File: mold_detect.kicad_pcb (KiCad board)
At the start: 2 copper layers, 37 x 70 mm, 26 parts, among them J1 USB_C_Receptacle_USB2.0_14P, U1 SHT30-DIS, U2 TPL5010, U3 ATmega328P-P, U4 W25Q128JVS, U5 FT230XS

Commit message: the spi flash chip works
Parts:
- added C10: 22pF, Capacitor_SMD:C_0603_1608Metric_Pad1.08x0.95mm_HandSolder, F.Cu at (123.5, 72.5)
- added C2: 47pF, Capacitor_SMD:C_0603_1608Metric_Pad1.08x0.95mm_HandSolder, F.Cu at (123.5, 57.4)
- added C3: 10nF, Capacitor_SMD:C_0603_1608Metric_Pad1.08x0.95mm_HandSolder, F.Cu at (123.5, 59.9)
- added C4: 47pF, Capacitor_SMD:C_0603_1608Metric_Pad1.08x0.95mm_HandSolder, F.Cu at (123.5, 62.4)
- added C5: 100n, Capacitor_SMD:C_0603_1608Metric_Pad1.08x0.95mm_HandSolder, F.Cu at (123.5, 64.9)
- added C6: 100n, Capacitor_SMD:C_0603_1608Metric_Pad1.08x0.95mm_HandSolder, F.Cu at (123.5, 67.4)
- added C9: 22pF, Capacitor_SMD:C_0603_1608Metric_Pad1.08x0.95mm_HandSolder, F.Cu at (123.5, 69.9)
- added R6: 27R, Resistor_SMD:R_0603_1608Metric_Pad0.98x0.95mm_HandSolder, F.Cu at (123.5, 75.0)
- added R7: 27R, Resistor_SMD:R_0603_1608Metric_Pad0.98x0.95mm_HandSolder, F.Cu at (123.5, 77.5)
- C3: value 100n -> 10nF
- renumbered C2 to C8, R6 to R10, R7 to R4, R8 to R5, R4 to R8, R5 to R9, U5 to U3, U3 to U5
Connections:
- C3 pad 2: +3V0 -> Net-(C3-Pad2)
- J1 pad A4: Net-(U5-VCC) -> Net-(C3-Pad2)
- J1 pad A6: Net-(U5-USBDM) -> Net-(C4-Pad2)
- J1 pad A7: Net-(U5-USBDP) -> Net-(C2-Pad2)
- J1 pad A9: Net-(U5-VCC) -> Net-(C3-Pad2)
- J1 pad B4: Net-(U5-VCC) -> Net-(C3-Pad2)
- J1 pad B6: Net-(U5-USBDM) -> Net-(C4-Pad2)
- J1 pad B7: Net-(U5-USBDP) -> Net-(C2-Pad2)
- J1 pad B9: Net-(U5-VCC) -> Net-(C3-Pad2)
- U3 pad 1: TXD -> RXD
- U3 pad 11: unconnected-(U5-~{RESET}-Pad11) -> +3V0
- U3 pad 12: Net-(U5-VCC) -> Net-(U3-VCC)
- U3 pad 4: RXD -> TXD
- U3 pad 8: Net-(U5-USBDP) -> Net-(U3-USBDP)
- U3 pad 9: Net-(U5-USBDM) -> Net-(U3-USBDM)
- U5 pad 10: unconnected-(U3-XTAL2/PB7-Pad10) -> Net-(U5-XTAL2/PB7)
- U5 pad 9: unconnected-(U3-XTAL1/PB6-Pad9) -> Net-(U5-XTAL1/PB6)
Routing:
- net (no net): track 0.00 -> 40.2 mm, vias 0 -> 2
- net Net-(U5-VCC): track 16.3 -> 0.00 mm, vias 2 -> 0
- net Net-(U5-USBDP): track 13.2 -> 0.00 mm
- net Net-(U5-USBDM): track 10.7 -> 0.00 mm

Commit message: tpl5010 works!
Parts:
- added C11: 100n, Capacitor_SMD:C_0603_1608Metric_Pad1.08x0.95mm_HandSolder, F.Cu at (141.6, 116.5)
- added D2: D_Schottky, Diode_SMD:D_SOD-323_HandSoldering, F.Cu at (142.0, 113.8)
- added J2: ISP, Connector_IDC:IDC-Header_2x03_P2.54mm_Vertical, F.Cu at (128.0, 112.0)
- added R11: 100R, Resistor_SMD:R_0603_1608Metric_Pad0.98x0.95mm_HandSolder, F.Cu at (141.6, 119.0)
- added Red2: LED, LED_THT:LED_D3.0mm, F.Cu at (141.1, 109.5)
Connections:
- net MISO renamed CIPO
- net MOSI renamed COPI
- Blue1 pad 2: TEMP_LED -> HUM_LED
- C3 pad 2: Net-(C3-Pad2) -> Net-(D2-K) (x2)
- J1 pad A4: Net-(C3-Pad2) -> Net-(D2-A)
- J1 pad A9: Net-(C3-Pad2) -> Net-(D2-A)
- J1 pad B4: Net-(C3-Pad2) -> Net-(D2-A)
- J1 pad B9: Net-(C3-Pad2) -> Net-(D2-A)
- R1 pad 1: Net-(Red1-K) -> GND
- R1 pad 2: GND -> Net-(Red2-K)
- R2 pad 1: Net-(Blue1-K) -> GND
- R2 pad 2: GND -> Net-(Blue1-K)
- Red1 pad 2: HUM_LED -> ERROR_LED
- U5 pad 13: unconnected-(U5-PD7-Pad13) -> ERROR_LED
- U5 pad 15: FLASH_CS -> unconnected-(U5-PB1-Pad15)
- U5 pad 16: unconnected-(U5-PB2-Pad16) -> FLASH_CS
- U5 pad 4: WAKE_INTR -> unconnected-(U5-PD2-Pad4)
- U5 pad 5: DONE -> WAKE_INTR
- U5 pad 6: unconnected-(U5-PD4-Pad6) -> DONE
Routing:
- net Net-(U3-VCC): track 0.00 -> 16.3 mm, vias 0 -> 2
- net (no net): track 40.2 -> 23.9 mm, vias 2 -> 0

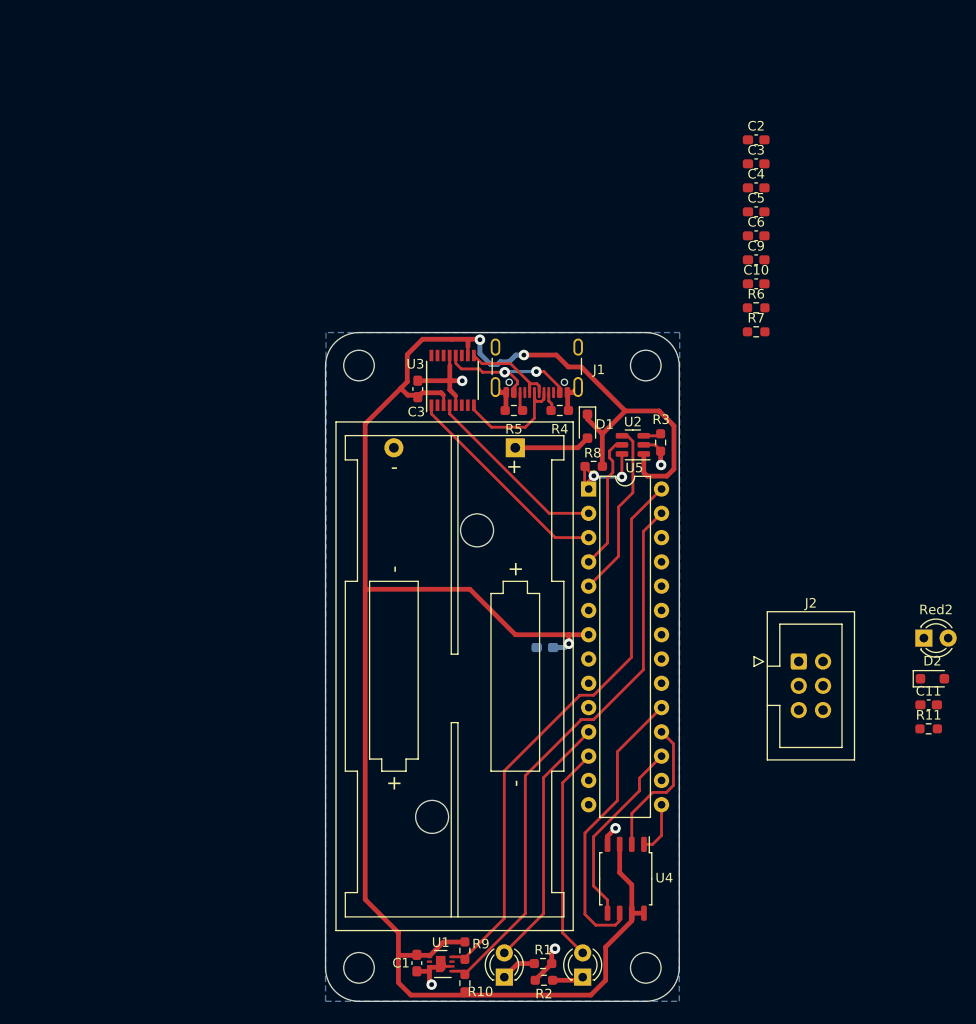
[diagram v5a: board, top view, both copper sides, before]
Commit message: updated footprints; started layout
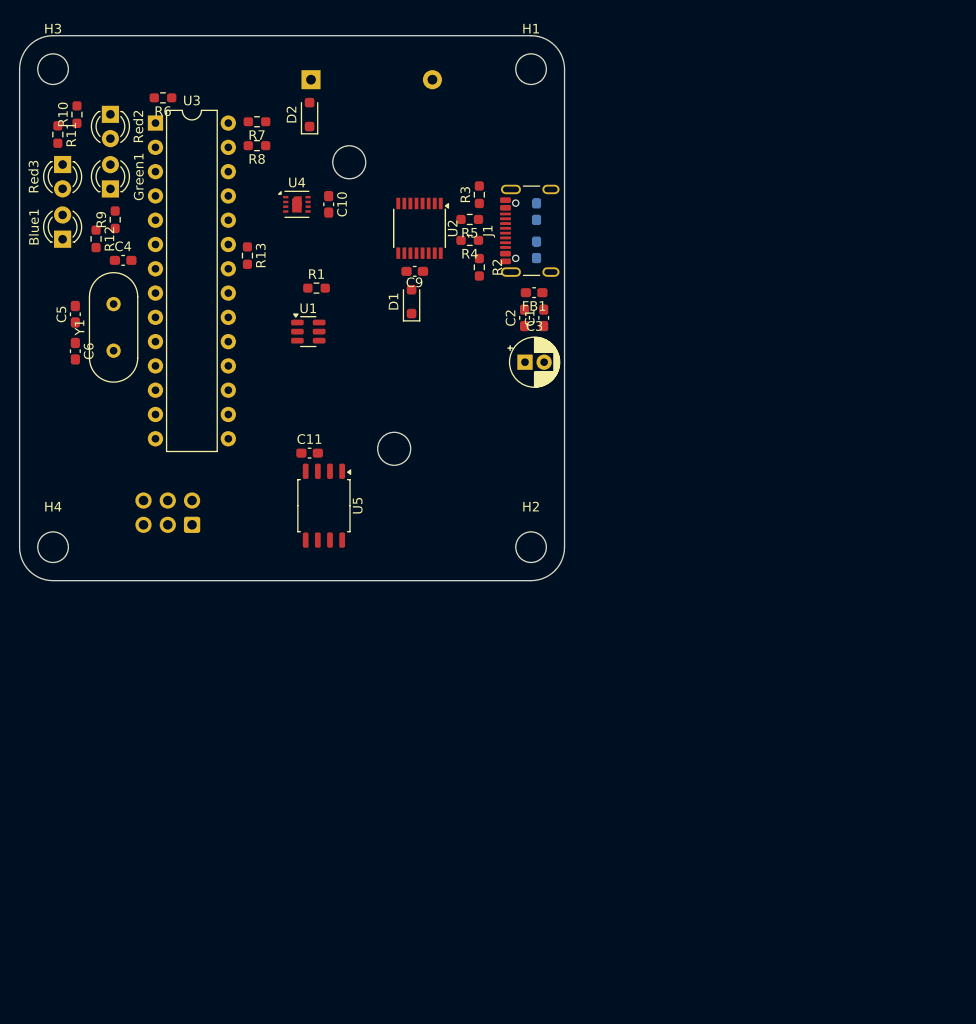
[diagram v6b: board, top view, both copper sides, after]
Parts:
- removed the C3 at (88.2, 83.5)
- removed the C3 at (123.5, 59.9)
- removed G***: LOGO, Library:kit_logo
- removed Red1: LED, LED_THT:LED_D3.0mm
- added C3: 4u7, Capacitor_THT:CP_Radial_D5.0mm_P2.00mm, F.Cu at (99.4, 80.7)
- added C7: 47pF, Capacitor_SMD:C_0603_1608Metric_Pad1.08x0.95mm_HandSolder, B.Cu at (100.6, 64.9)
- added FB1: ~, Capacitor_SMD:C_0603_1608Metric_Pad1.08x0.95mm_HandSolder, F.Cu at (100.3, 73.4)
- added Green1: LED, LED_THT:LED_D3.0mm, F.Cu at (56.0, 62.5)
- added R12: 100R, Resistor_SMD:R_0603_1608Metric_Pad0.98x0.95mm_HandSolder, F.Cu at (54.5, 67.8)
- added R13: 10k, Resistor_SMD:R_0603_1608Metric_Pad0.98x0.95mm_HandSolder, F.Cu at (70.3, 69.5)
- added Red3: LED, LED_THT:LED_D3.0mm, F.Cu at (51.0, 60.0)
- added Y1: 16MHz, Crystal:Crystal_HC49-4H_Vertical, F.Cu at (56.3, 79.5)
- BT1, J2: moved to B.Cu
- C1: value 100n -> 10nF
- C10, C9: value 22pF -> 100n
- C2, C4: value 47pF -> 100n
- C5, C6: value 100n -> 22pF
- C8: value 100n -> 47pF
- R1: value 100R -> 22k021
- R10, R9: value 10k -> 100R
- R2: value 100R -> 5k1
- R3: value 22k021 -> 5k1
- R4, R5: value 5k1 -> 27R
- R6, R7: value 27R -> 10k
- U1: value SHT30-DIS -> TPL5010; footprint Sensor_Humidity:Sensirion_DFN-8-1EP_2.5x2.5mm_P0.5mm_EP1.1x1.7mm -> Package_TO_SOT_SMD:SOT-23-6
- U2: value TPL5010 -> FT230XS; footprint Package_TO_SOT_SMD:SOT-23-6 -> Package_SO:SSOP-16_3.9x4.9mm_P0.635mm
- U3: value FT230XS -> ATmega328P-P; footprint Package_SO:SSOP-16_3.9x4.9mm_P0.635mm -> Package_DIP:DIP-28_W7.62mm
- U4: value W25Q128JVS -> SHT30-DIS; footprint Package_SO:SOIC-8_5.23x5.23mm_P1.27mm -> Sensor_Humidity:Sensirion_DFN-8-1EP_2.5x2.5mm_P0.5mm_EP1.1x1.7mm
- U5: value ATmega328P-P -> W25Q128JVS; footprint Package_DIP:DIP-28_W7.62mm -> Package_SO:SOIC-8_5.23x5.23mm_P1.27mm
- moved H3 112.6 mm to (50.0, 50.0)
- moved R11 110.3 mm to (50.5, 56.8), turned to -90 degrees
- moved Red2 101.2 mm to (56.0, 54.7), turned to -90 degrees
- moved R10 99.5 mm to (52.5, 54.8)
- moved H1 95.7 mm to (100.0, 50.0)
- moved Blue1 94.4 mm to (51.0, 67.8)
- moved D2 87.9 mm to (76.8, 54.8), turned to 90 degrees
- moved R9 84.7 mm to (56.5, 65.8), turned to 90 degrees
- moved U4 78.5 mm to (75.5, 64.1), turned to 0 degrees
- moved R2 74.9 mm to (94.6, 70.7), turned to -90 degrees
- moved R1 74.5 mm to (77.6, 72.9)
- moved C6 72.2 mm to (52.3, 79.5), turned to -90 degrees
- moved C5 72.0 mm to (52.3, 75.6), turned to 90 degrees
- moved C11 69.9 mm to (76.8, 90.2)
- moved C1 68.8 mm to (101.3, 76.0)
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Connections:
- C1 pad 2: +3V0 -> Net-(C1-Pad2)
- C10 pad 2: Net-(U5-XTAL2/PB7) -> +3V0
- C2 pad 2: Net-(C2-Pad2) -> Net-(U2-VCC)
- C4 pad 2: Net-(C4-Pad2) -> +3V0
- C5 pad 2: +3V0 -> Net-(U3-XTAL1/PB6)
- C6 pad 2: Net-(U3-VCC) -> Net-(U3-XTAL2/PB7)
- C8 pad 2: +3V0 -> Net-(C8-Pad2)
- C9 pad 2: Net-(U5-XTAL1/PB6) -> USB_ENABLE_INTR
- D1 pad 2: Net-(BT1-+) -> USB_ENABLE_INTR
- D2 pad 1: Net-(D2-K) -> +3V0
- D2 pad 2: Net-(D2-A) -> Net-(BT1-+)
- J1 pad A4: Net-(D2-A) -> Net-(C1-Pad2)
- J1 pad A6: Net-(C4-Pad2) -> Net-(C8-Pad2)
- J1 pad A7: Net-(C2-Pad2) -> Net-(C7-Pad2)
- J1 pad A9: Net-(D2-A) -> Net-(C1-Pad2)
- J1 pad B4: Net-(D2-A) -> Net-(C1-Pad2)
- J1 pad B6: Net-(C4-Pad2) -> Net-(C8-Pad2)
- J1 pad B7: Net-(C2-Pad2) -> Net-(C7-Pad2)
- J1 pad B9: Net-(D2-A) -> Net-(C1-Pad2)
- R1 pad 1: GND -> Net-(U1-DELAY/M_RST)
- R1 pad 2: Net-(Red2-K) -> GND
- R10 pad 1: +3V0 -> GND
- R10 pad 2: SDA -> Net-(Red2-K)
- R2 pad 1: GND -> Net-(J1-CC1)
- R2 pad 2: Net-(Blue1-K) -> GND
- R3 pad 1: Net-(U2-DELAY/M_RST) -> Net-(J1-CC2)
- R4 pad 1: Net-(J1-CC1) -> Net-(C7-Pad2)
- R4 pad 2: GND -> Net-(U2-USBDM)
- R5 pad 1: Net-(J1-CC2) -> Net-(C8-Pad2)
- R5 pad 2: GND -> Net-(U2-USBDP)
- R6 pad 1: Net-(C2-Pad2) -> +3V0
- R6 pad 2: Net-(U3-USBDM) -> RST
- R7 pad 1: Net-(C4-Pad2) -> +3V0
- R7 pad 2: Net-(U3-USBDP) -> SCL
- R8 pad 2: RST -> SDA
- R9 pad 1: +3V0 -> GND
- R9 pad 2: SCL -> Net-(Green1-K)
- Red2 pad 2: TEMP_LED -> ERROR_LED
- U1 pad 1: SDA -> +3V0
- U1 pad 3: unconnected-(U1-ALERT-Pad3) -> Net-(U1-DELAY/M_RST)
- U1 pad 4: SCL -> DONE
- U1 pad 5: +3V0 -> WAKE_INTR
- U1 pad 6: unconnected-(U1-~{RESET}-Pad6) -> RST
- U2 pad 1: +3V0 -> RXD
- U2 pad 2: GND -> unconnected-(U2-~{RTS}-Pad2)
- U2 pad 3: Net-(U2-DELAY/M_RST) -> USB_ENABLE_INTR
- U2 pad 4: DONE -> TXD
- U2 pad 5: WAKE_INTR -> GND
- U2 pad 6: RST -> unconnected-(U2-~{CTS}-Pad6)
- U3 pad 1: RXD -> RST
- U3 pad 10: +3V0 -> Net-(U3-XTAL2/PB7)
- U3 pad 11: +3V0 -> HUM_LED
- U3 pad 12: Net-(U3-VCC) -> TEMP_LED
- U3 pad 13: GND -> ERROR_LED
- U3 pad 16: unconnected-(U3-CBUS3-Pad16) -> FLASH_CS
- U3 pad 2: unconnected-(U3-~{RTS}-Pad2) -> RXD
- U3 pad 3: +3V0 -> TXD
- U3 pad 4: TXD -> GENERAL_LED
- U3 pad 5: GND -> WAKE_INTR
- U3 pad 6: unconnected-(U3-~{CTS}-Pad6) -> DONE
- U3 pad 7: unconnected-(U3-CBUS2-Pad7) -> +3V0
- U3 pad 8: Net-(U3-USBDP) -> GND
- U3 pad 9: Net-(U3-USBDM) -> Net-(U3-XTAL1/PB6)
- U4 pad 1: FLASH_CS -> SDA
- U4 pad 2: CIPO -> GND
- U4 pad 3: +3V0 -> unconnected-(U4-ALERT-Pad3)
- U4 pad 4: GND -> SCL
- U4 pad 5: COPI -> +3V0
- U4 pad 6: SCK -> unconnected-(U4-~{RESET}-Pad6)
- U4 pad 7: +3V0 -> GND
- U4 pad 8: +3V0 -> GND
- U5 pad 1: RST -> FLASH_CS
- U5 pad 2: RXD -> CIPO
- U5 pad 3: TXD -> +3V0
- U5 pad 4: unconnected-(U5-PD2-Pad4) -> GND
- U5 pad 5: WAKE_INTR -> COPI
- U5 pad 6: DONE -> SCK
- U5 pad 8: GND -> +3V0
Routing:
- net +3V0: track 206.1 -> 0.00 mm, vias 3 -> 0
- net SCL: track 60.0 -> 0.00 mm
- net SDA: track 58.9 -> 0.00 mm
- net GND: track 32.7 -> 0.00 mm, vias 5 -> 0
- net SCK: track 30.0 -> 0.00 mm
- net HUM_LED: track 26.8 -> 0.00 mm
- net (no net): track 23.9 -> 0.00 mm
- net TXD: track 22.8 -> 0.00 mm
- net TEMP_LED: track 22.6 -> 0.00 mm
- net COPI: track 20.0 -> 0.00 mm
- net RXD: track 19.8 -> 0.00 mm
- net DONE: track 18.8 -> 0.00 mm
- net Net-(U3-VCC): track 16.3 -> 0.00 mm, vias 2 -> 0
- net CIPO: track 14.9 -> 0.00 mm
- net WAKE_INTR: track 14.4 -> 0.00 mm
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- removed copper zone on B.Cu, net GND
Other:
- board size 37 x 70 mm -> 57 x 57 mm
- board text removed: "github.com/christopher-besch/mold_detect Christopher Besch <mail@chris-besch.com> designed at the Chair for Embedded Systems Rev. 1.0.0 January 2024"

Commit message: updated PCB design
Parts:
- removed Red3: LED, LED_THT:LED_D3.0mm
- added C12: 100n, Capacitor_SMD:C_0603_1608Metric_Pad1.08x0.95mm_HandSolder, F.Cu at (82.5, 81.0)
- added G***: LOGO, Library:kit_logo, B.Cu at (95.0, 93.5)
- added Red1: LED, LED_THT:LED_D3.0mm, F.Cu at (51.0, 60.0)
- C5: value 22pF -> 100n; moved to B.Cu
- C7: value 47pF -> 22pF; moved to F.Cu
- C9: value 100n -> 47pF; moved to B.Cu
- J2: moved to F.Cu
- R13: value 10k -> 100R
- R9: value 100R -> 10k
- moved C7 50.1 mm to (52.7, 79.5)
- moved C11 33.7 mm to (74.5, 56.5), turned to 90 degrees
- moved C4 19.4 mm to (76.5, 73.0)
- moved R6 18.9 mm to (70.5, 69.6), turned to -90 degrees
- moved R9 16.9 mm to (71.5, 58.0), turned to 180 degrees
- moved R13 16.0 mm to (54.5, 67.5)
- moved C9 14.1 mm to (100.5, 65.0), turned to -90 degrees
- moved U5 13.1 mm to (76.9, 82.6), turned to 180 degrees
- moved R12 12.5 mm to (52.5, 55.4), turned to 90 degrees
- moved C5 11.8 mm to (63.5, 71.9)
- moved R10 11.5 mm to (56.5, 65.5)
- moved C10 11.5 mm to (88.0, 71.0), turned to 180 degrees
- moved R7 10.1 mm to (61.5, 53.0)
- moved U4 8.18 mm to (77.7, 56.2), turned to 180 degrees
- moved J2 5.05 mm to (59.5, 98.0)
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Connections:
- C10 pad 2: +3V0 -> USB_ENABLE_INTR
- C5 pad 2: Net-(U3-XTAL1/PB6) -> +3V0
- C6 pad 2: Net-(U3-XTAL2/PB7) -> Net-(U3-XTAL1/PB6)
- C7 pad 2: Net-(C7-Pad2) -> Net-(U3-XTAL2/PB7)
- C9 pad 2: USB_ENABLE_INTR -> Net-(C9-Pad2)
- J1 pad A6: Net-(C8-Pad2) -> Net-(C9-Pad2)
- J1 pad A7: Net-(C7-Pad2) -> Net-(C8-Pad2)
- J1 pad B6: Net-(C8-Pad2) -> Net-(C9-Pad2)
- J1 pad B7: Net-(C7-Pad2) -> Net-(C8-Pad2)
- R10 pad 2: Net-(Red2-K) -> Net-(Green1-K)
- R12 pad 2: Net-(Blue1-K) -> Net-(Red2-K)
- R13 pad 1: USB_ENABLE_INTR -> GND
- R13 pad 2: GND -> Net-(Blue1-K)
- R4 pad 1: Net-(C7-Pad2) -> Net-(C8-Pad2)
- R5 pad 1: Net-(C8-Pad2) -> Net-(C9-Pad2)
- R6 pad 1: +3V0 -> USB_ENABLE_INTR
- R6 pad 2: RST -> GND
- R7 pad 2: SCL -> RST
- R8 pad 2: SDA -> SCL
- R9 pad 1: GND -> +3V0
- R9 pad 2: Net-(Green1-K) -> SDA
- Red2 pad 2: ERROR_LED -> TEMP_LED
- U3 pad 11: HUM_LED -> GENERAL_LED
- U3 pad 12: TEMP_LED -> HUM_LED
- U3 pad 4: GENERAL_LED -> TEMP_LED
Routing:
- net +3V0: track 0.00 -> 135.4 mm, vias 0 -> 7
- net RST: track 0.00 -> 82.8 mm, vias 0 -> 4
- net GND: track 0.00 -> 55.3 mm, vias 0 -> 7
- net GENERAL_LED: track 0.00 -> 35.9 mm
- net SCK: track 0.00 -> 35.9 mm
- net CIPO: track 0.00 -> 35.7 mm
- net ERROR_LED: track 0.00 -> 34.3 mm
- net COPI: track 0.00 -> 33.1 mm, vias 0 -> 2
- net RXD: track 0.00 -> 32.8 mm
- net USB_ENABLE_INTR: track 0.00 -> 30.6 mm, vias 0 -> 2
- net TXD: track 0.00 -> 29.9 mm
- net HUM_LED: track 0.00 -> 29.0 mm
- net WAKE_INTR: track 0.00 -> 27.3 mm
- net DONE: track 0.00 -> 26.0 mm
- net Net-(U2-VCC): track 0.00 -> 21.8 mm
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- added copper zone on F.Cu, net (none)
- added copper zone on B.Cu, net GND
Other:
- board text added: "ISP"
- board text added: "Rev. 2.0.0 April 2024"
- board text added: "USB-C"
- board text added: "designed at the Chair for Embedded Systems"
- board text added: "github.com/christopher-besch/mold_detect"
- board text added: "made in Germany by Christopher Besch <mail@chris-besch.com>"

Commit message: added blender
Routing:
- added copper zone on F.Cu, net GND
- removed copper zone on F.Cu, net (none)
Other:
- board text added: "PCB3D_BR_mainboard"
- board text added: "PCB3D_TL_mainboard"
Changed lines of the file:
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@@
 		(tags "capacitor handsolder")
 		(property "Reference" "C4"
-			(at 0 -1.43 360)
+			(at 0 -1.43 0)
 			(layer "F.SilkS")
 			(effects
@@
 		)
 		(property "Value" "100n"
-			(at 0 1.43 360)
+			(at 0 1.43 0)
 			(layer "F.Fab")
 			(effects
@@
 		)
 		(fp_text user "${REFERENCE}"
-			(at 0 0 360)
+			(at 0 0 0)
 			(layer "F.Fab")
 			(effects
@@
 		(tags "SOT TO_SOT_SMD")
 		(property "Reference" "U1"
-			(at 0 -2.4 360)
+			(at 0 -2.4 0)
 			(layer "F.SilkS")
 			(effects
@@
 		)
 		(property "Value" "TPL5010"
-			(at 0 2.4 360)
+			(at 0 2.4 0)
 			(layer "F.Fab")
 			(effects
@@
 		)
 		(fp_text user "${REFERENCE}"
-			(at 0 0 360)
+			(at 0 0 0)
 			(layer "F.Fab")
 			(effects
@@
 		(tags "resistor handsolder")
 		(property "Reference" "R1"
-			(at 0 -1.43 270)
+			(at 0 -1.43 -90)
 			(layer "F.SilkS")
 			(effects
@@
 		)
 		(property "Value" "22k021"
-			(at 0 1.43 270)
+			(at 0 1.43 -90)
 			(layer "F.Fab")
 			(effects
@@
 		)
 		(fp_text user "${REFERENCE}"
-			(at 0 0 270)
+			(at 0 0 -90)
 			(layer "F.Fab")
 			(effects
@@
 		)
 		(property "Value" "D_Schottky"
-			(at 0.1 1.9 270)
+			(at 0.1 1.9 -90)
 			(layer "F.Fab")
 			(effects
@@
 		)
 		(fp_text user "${REFERENCE}"
-			(at 0 -1.85 270)
+			(at 0 -1.85 -90)
 			(layer "F.Fab")
 			(effects
@@
 		(tags "SOD-323")
 		(property "Reference" "D2"
-			(at 0 -1.85 270)
+			(at 0 -1.85 -90)
 			(layer "F.SilkS")
 			(effects
@@
 		)
 		(property "Value" "D_Schottky"
-			(at 0.1 1.9 270)
+			(at 0.1 1.9 -90)
 			(layer "F.Fab")
 			(effects
@@
 		)
 		(fp_text user "${REFERENCE}"
-			(at 0 -1.85 270)
+			(at 0 -1.85 -90)
 			(layer "F.Fab")
 			(effects
@@
 		(tags "capacitor handsolder")
 		(property "Reference" "C6"
-			(at 2.43 -0.1675 360)
+			(at 2.43 -0.1675 0)
 			(layer "F.SilkS")
 			(effects
@@
 		)
 		(property "Value" "22pF"
-			(at 0 1.43 270)
+			(at 0 1.43 -90)
 			(layer "F.Fab")
 			(effects
@@
 		)
 		(fp_text user "${REFERENCE}"
-			(at 0 0 270)
+			(at 0 0 -90)
 			(layer "F.Fab")
 			(effects
@@
 		(tags "Through hole vertical IDC box header THT 2x03 2.54mm double row")
 		(property "Reference" "J2"
-			(at 7.5 -2.5 270)
+			(at 7.5 -2.5 -90)
 			(layer "F.Fab")
 			(effects
@@
 		)
 		(property "Value" "ISP"
-			(at 1.27 11.18 270)
+			(at 1.27 11.18 -90)
 			(layer "F.Fab")
 			(effects
@@
 		)
 		(property "Value" "100n"
-			(at 0 1.43 270)
+			(at 0 1.43 -90)
 			(layer "F.Fab")
 			(effects
@@
 		)
 		(fp_text user "${REFERENCE}"
-			(at 0 0 270)
+			(at 0 0 -90)
 			(layer "F.Fab")
 			(effects
@@
 		)
 		(property "Value" "100R"
-			(at 0 1.43 270)
+			(at 0 1.43 -90)
 			(layer "F.Fab")
 			(effects
@@
 		)
 		(fp_text user "${REFERENCE}"
-			(at 0 0 270)
+			(at 0 0 -90)
 			(layer "F.Fab")
 			(effects
@@
 		(tags "resistor handsolder")
 		(property "Reference" "R12"
-			(at 2.4125 1 360)
+			(at 2.4125 1 0)
 			(layer "F.SilkS")
 			(effects
@@
 		)
 		(property "Value" "100R"
-			(at 0 1.43 270)
+			(at 0 1.43 -90)
 			(layer "F.Fab")
 			(effects
@@
 		)
 		(fp_text user "${REFERENCE}"
-			(at 0 0 270)
+			(at 0 0 -90)
 			(layer "F.Fab")
 			(effects
@@
 		(tags "LED diameter 3.0mm 2 pins")
 		(property "Reference" "Green1"
-			(at 1.27 3 270)
+			(at 1.27 3 -90)
 			(layer "F.SilkS")
 			(effects
@@
 		)
 		(property "Value" "LED"
-			(at 1.27 2.96 270)
+			(at 1.27 2.96 -90)
 			(layer "F.Fab")
 			(effects
@@
 		)
 		(property "Value" "5k1"
-			(at 0 1.43 270)
+			(at 0 1.43 -90)
 			(layer "F.Fab")
 			(effects
@@
 		)
 		(fp_text user "${REFERENCE}"
-			(at 0 0 270)
+			(at 0 0 -90)
 			(layer "F.Fab")
 			(effects
@@
 		)
 		(property "Value" "16MHz"
-			(at 2.44 3.525 270)
+			(at 2.44 3.525 -90)
 			(layer "F.Fab")
 			(effects
@@
 		)
 		(fp_text user "${REFERENCE}"
-			(at 2.44 0 270)
+			(at 2.44 0 -90)
 			(layer "F.Fab")
 			(effects
@@
 		(tags "LED diameter 3.0mm 2 pins")
 		(property "Reference" "Blue1"
-			(at 1.27 -2.96 270)
+			(at 1.27 -2.96 -90)
 			(layer "F.SilkS")
 			(effects
@@
 		)
 		(property "Value" "LED"
-			(at 1.27 2.96 270)
+			(at 1.27 2.96 -90)
 			(layer "F.Fab")
 			(effects
@@
 		)
 		(property "Value" "100n"
-			(at 0 -1.43 270)
+			(at 0 -1.43 -90)
 			(layer "B.Fab")
 			(effects
@@
 		)
 		(fp_text user "${REFERENCE}"
-			(at 0 0 270)
+			(at 0 0 -90)
 			(layer "B.Fab")
 			(effects
@@
 		)
 		(property "Value" "47pF"
-			(at 0 -1.43 270)
+			(at 0 -1.43 -90)
 			(layer "B.Fab")
 			(effects
@@
 		)
 		(fp_text user "${REFERENCE}"
-			(at 0 0 270)
+			(at 0 0 -90)
 			(layer "B.Fab")
 			(effects
@@
 		)
 	)
+	(gr_text "PCB3D_BR_mainboard"
+		(at 103.5 103.5 0)
+		(layer "F.Fab")
+		(effects
+			(font
+				(size 1.5 1.5)
+				(thickness 0.3)
+				(bold yes)
+			)
+			(justify left bottom)
+		)
+	)
+	(gr_text "PCB3D_TL_mainboard"
+		(at 46.5 46.5 0)
+		(layer "F.Fab")
+		(effects
+			(font
+				(size 1.5 1.5)
+				(thickness 0.3)
+				(bold yes)
+			)
+			(justify left bottom)
+		)
+	)
 	(segment
 		(start 51.6225 68.4125)
@@
 	)
 	(zone
-		(net 0)
-		(net_name "")
+		(net 10)
+		(net_name "GND")
 		(layer "F.Cu")
 		(hatch edge 0.5)
@@
 			(thermal_gap 0.5)
 			(thermal_bridge_width 0.5)
-			(island_removal_mode 1)
-			(island_area_min 10)
 		)
 		(polygon
